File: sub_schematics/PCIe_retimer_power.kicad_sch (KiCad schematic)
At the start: 35 parts

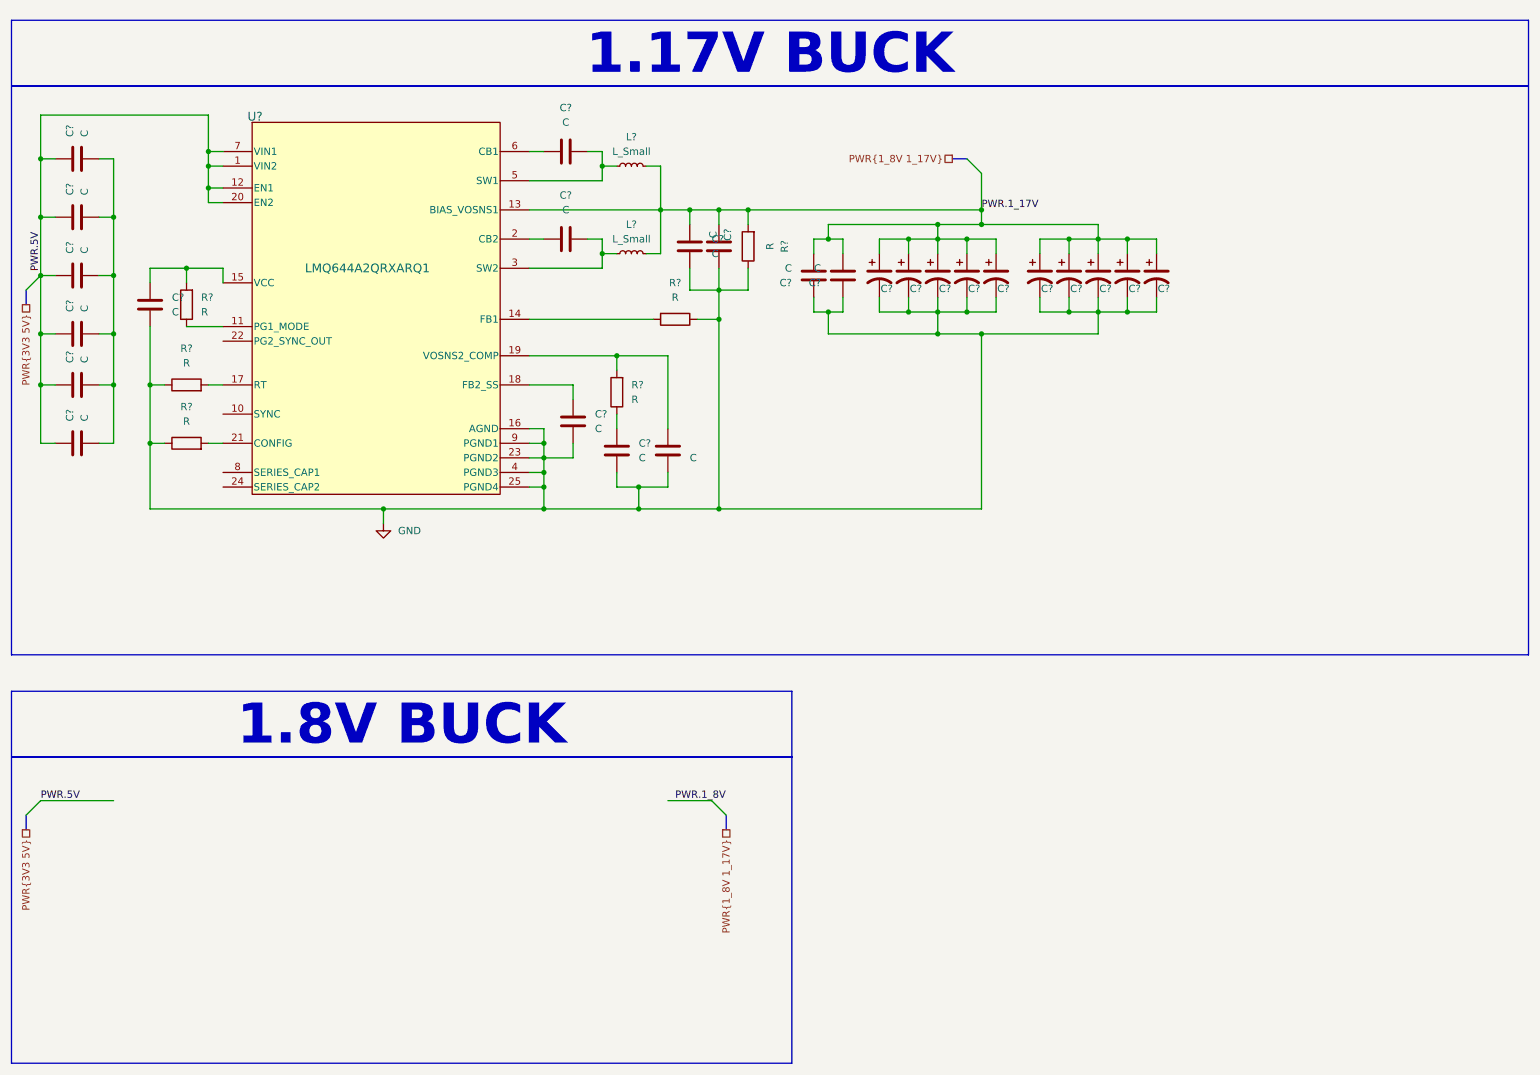
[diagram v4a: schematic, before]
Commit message: Schematics revamped
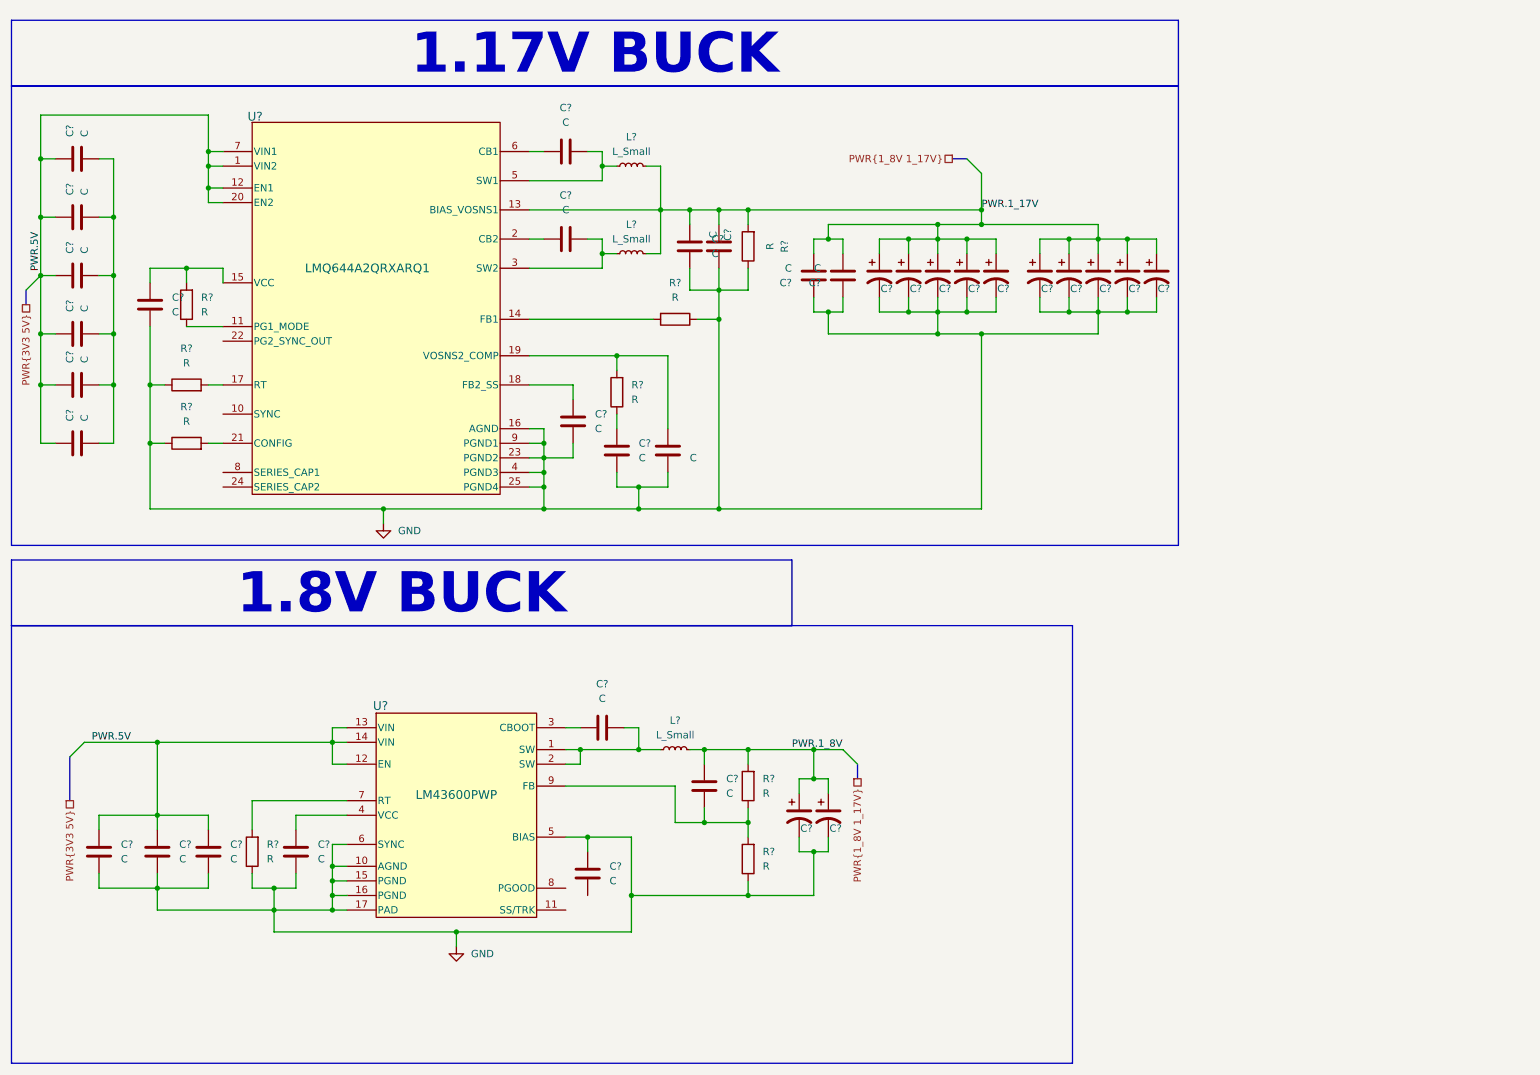
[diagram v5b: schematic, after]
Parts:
- added C? (x7): C, symbol Device:C
- added C? (x2): C_Polarized_US, symbol Device:C_Polarized_US
- added L?: L_Small, symbol Device:L_Small
- added R? (x3): R, symbol Device:R
- added U?: LM43600PWP, step-down-converter-1.8V:PWP0016F, symbol step-down-converter-1.8V:LM43600PWP
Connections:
- net GND: now also C?.1, C?.2, C?.2, C?.2, C?.2, C?.2, C?.2, R?.1, R?.1, U?.10 (AGND), U?.15 (PGND), U?.16 (PGND), U?.17 (PAD), U?.5 (BIAS), U?.6 (SYNC)
- net PWR.1_8V: now also C?.1, C?.1, C?.2, L?.2, R?.2
- net PWR.5V: now also C?.1, C?.1, C?.1, U?.12 (EN), U?.13 (VIN), U?.14 (VIN)
- new net: R?.2, U?.7 (RT)
- new net: C?.1, U?.3 (CBOOT)
- new net: C?.2, L?.1, U?.1 (SW), U?.2 (SW)
- new net: C?.1, R?.1, R?.2, U?.9 (FB)
- new net: C?.1, U?.4 (VCC)
